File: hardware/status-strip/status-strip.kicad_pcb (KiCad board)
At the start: 2 copper layers, 111 x 11 mm, 13 parts, among them J1 Conn_01x03

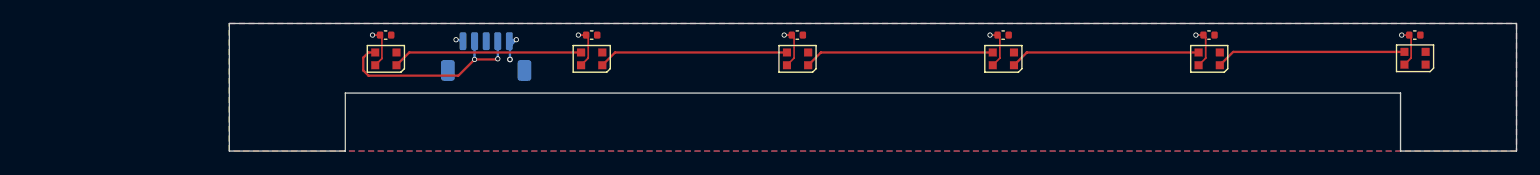
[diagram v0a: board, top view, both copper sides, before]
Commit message: feat(status-strip): add system-level status led
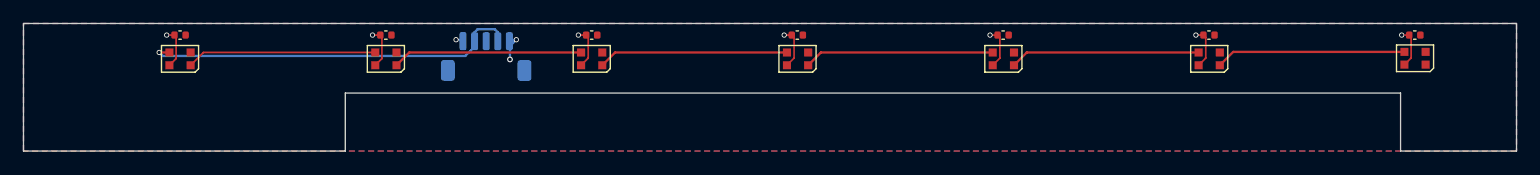
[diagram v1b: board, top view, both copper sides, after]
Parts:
- added C2: 100nF, Local Library:C_0402_1005Metric, F.Cu at (43.5, 25.0)
- added D2: WS2812C-2020-V6, Local Library:LED_WS2812B-2020_PLCC4_2.0x2.0mm, F.Cu at (43.5, 27.1)
- J1: value Conn_01x03 -> STATUS_LED
- moved D1 17.8 mm to (25.8, 27.1)
- moved C1 17.7 mm to (25.8, 25.0)
- renumbered C31 to C1, C32 to C3, C33 to C4, C34 to C5, C35 to C6, C36 to C7, D4 to D1, D5 to D3, D6 to D4, D7 to D5, D8 to D6, D9 to D7
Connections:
- D1 pad 1: Net-(D4-DOUT) (its old number) -> Net-(D1-DOUT)
- D3 pad 3: Net-(D4-DOUT) (its old number) -> Net-(D2-DOUT)
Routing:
- net Net-(D4-DOUT) (its old number): track 16.4 -> 0.00 mm
- net Net-(D2-DOUT): track 0.00 -> 16.4 mm
- net Net-(D1-DOUT): track 0.00 -> 16.4 mm
- net /LED_DATA: track 17.6 -> 32.8 mm, vias 2 -> 1
- net +5V: track 21.4 -> 25.0 mm, vias 6 -> 7
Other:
- board size 111 x 11 mm -> 128.8 x 11 mm
